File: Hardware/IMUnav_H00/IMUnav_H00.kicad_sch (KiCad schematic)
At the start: 11 parts, among them U7 STM32G474VETx

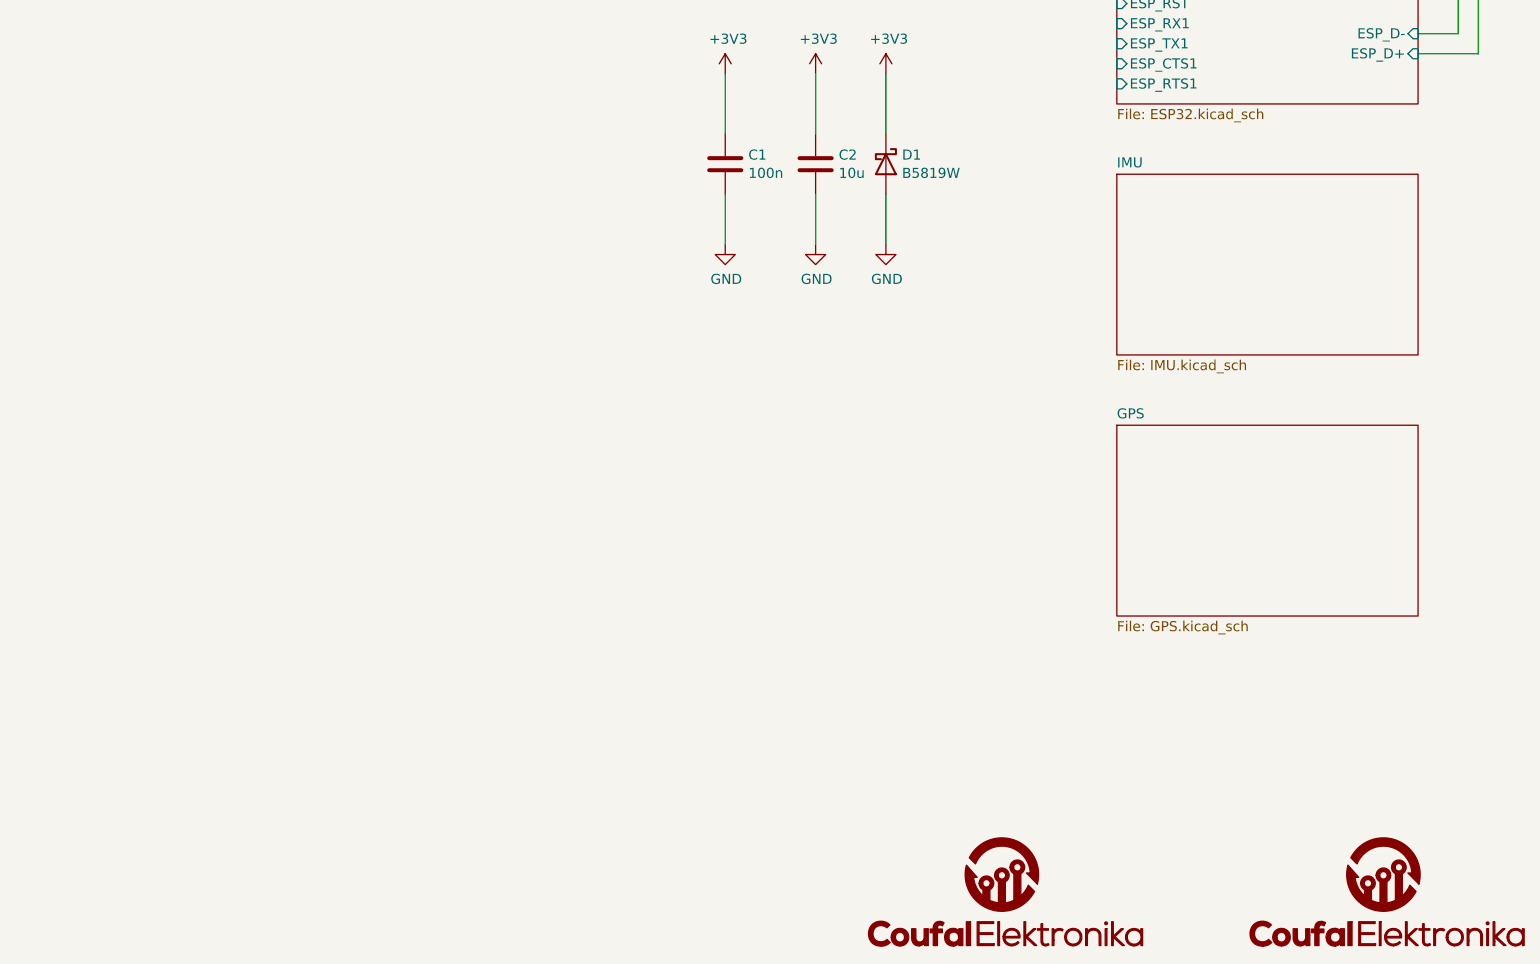
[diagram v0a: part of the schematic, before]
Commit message: Added IMU connection, created symbol for ADIS16505 PCB version
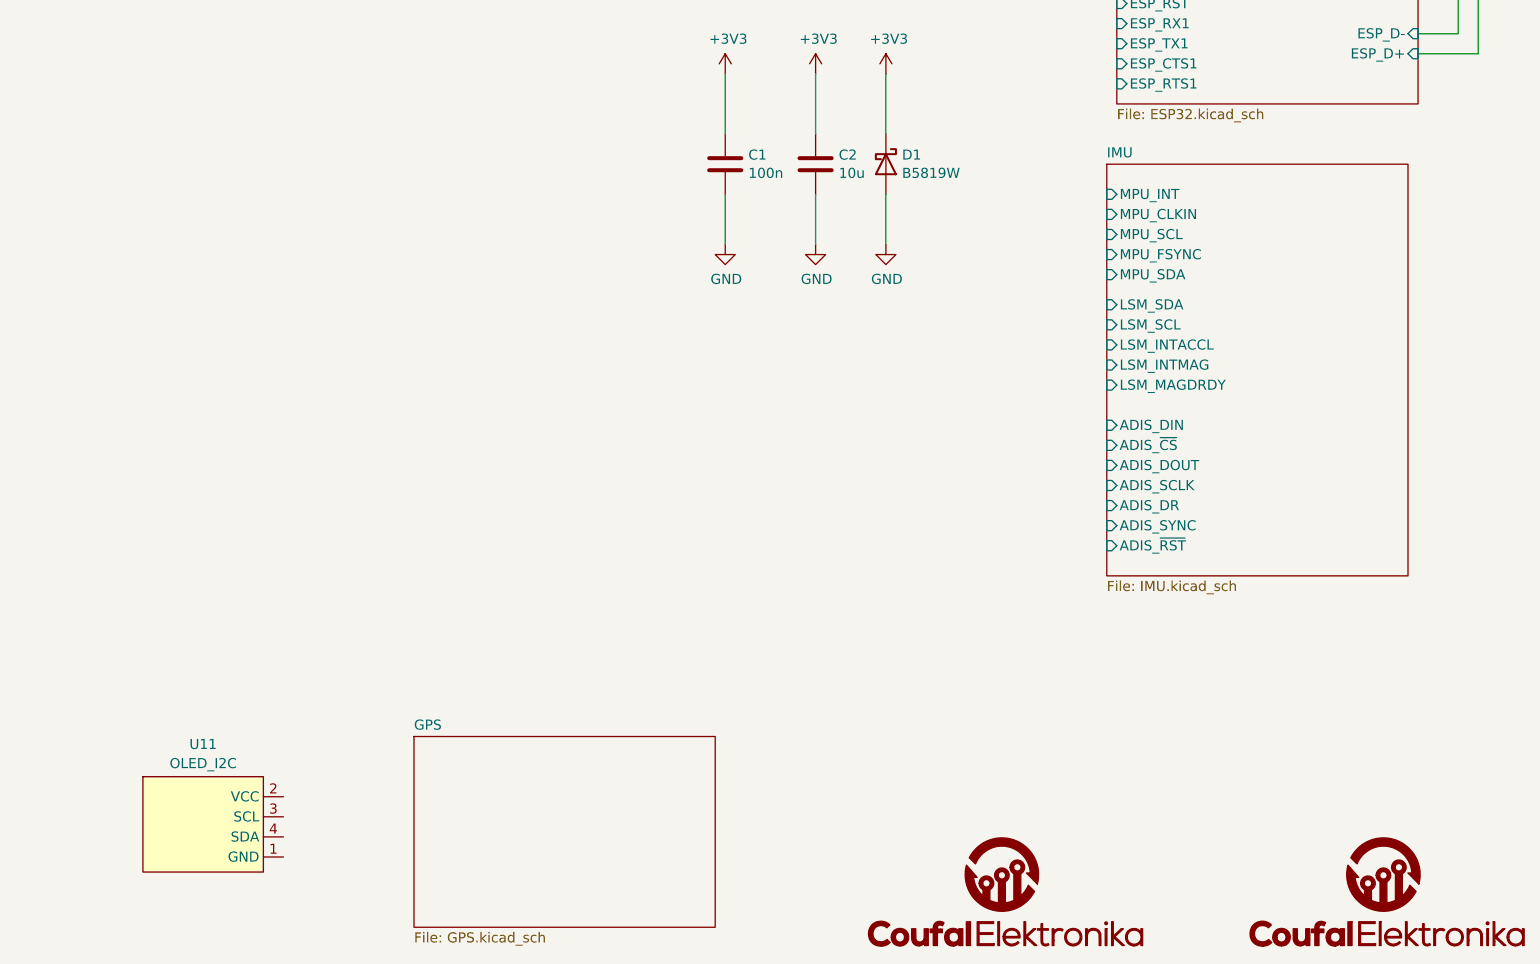
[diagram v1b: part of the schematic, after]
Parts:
- added U11: OLED_I2C, IMUnav:Display_128x64_096_I2C, symbol IMUnav:OLED_I2C
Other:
- sheet IMU ports: added ADIS_DIN, ADIS_DOUT, ADIS_DR, ADIS_SCLK, ADIS_SYNC, ADIS_~{CS}, ADIS_~{RST}, LSM_INTACCL, LSM_INTMAG, LSM_MAGDRDY, LSM_SCL, LSM_SDA, MPU_CLKIN, MPU_FSYNC, MPU_INT, MPU_SCL, MPU_SDA; removed none
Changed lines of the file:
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@@
+    )
+  )
+  (symbol (lib_id "IMUnav:OLED_I2C") (at 110.49 165.1 0) (unit 1)
+    (in_bom yes) (on_board yes) (dnp no) (fields_autoplaced)
+    (property "Reference" "U11" (at 109.22 154.6565 0)
+      (effects (font (size 1.27 1.27)))
+    )
+    (property "Value" "OLED_I2C" (at 109.22 157.0807 0)
+      (effects (font (size 1.27 1.27)))
+    )
+    (property "Footprint" "IMUnav:Display_128x64_096_I2C" (at 95.885 159.385 0)
+      (effects (font (size 1.27 1.27)) hide)
+    )
+    (property "Datasheet" "" (at 95.885 159.385 0)
+      (effects (font (size 1.27 1.27)) hide)
+    )
+    (pin "1")
+    (pin "2")
+    (pin "3")
+    (pin "4")
+    (instances
+      (project "IMUnav_H00"
+        (path "/4c2dd95e-3649-4040-ab57-00df6d22e0b0"
+          (reference "U11") (unit 1)
+        )
+      )
     )
   )
@@
     )
   )
-  (sheet (at 224.79 82.55) (size 38.1 22.86) (fields_autoplaced)
+  (sheet (at 223.52 81.28) (size 38.1 52.07) (fields_autoplaced)
     (stroke (width 0.1524) (type solid))
     (fill (color 0 0 0 0.0000))
-    (property "Sheetname" "IMU" (at 224.79 81.8384 0)
+    (property "Sheetname" "IMU" (at 223.52 80.5684 0)
       (effects (font (size 1.27 1.27)) (justify left bottom))
     )
-    (property "Sheetfile" "IMU.kicad_sch" (at 224.79 105.9946 0)
+    (property "Sheetfile" "IMU.kicad_sch" (at 223.52 133.9346 0)
       (effects (font (size 1.27 1.27)) (justify left top))
     )
+    (pin "MPU_CLKIN" input (at 223.52 87.63 180)
+      (effects (font (size 1.27 1.27)) (justify left))
+    )
+    (pin "MPU_SCL" input (at 223.52 90.17 180)
+      (effects (font (size 1.27 1.27)) (justify left))
+    )
+    (pin "MPU_FSYNC" input (at 223.52 92.71 180)
+      (effects (font (size 1.27 1.27)) (justify left))
+    )
+    (pin "MPU_SDA" input (at 223.52 95.25 180)
+      (effects (font (size 1.27 1.27)) (justify left))
+    )
+    (pin "LSM_SDA" input (at 223.52 99.06 180)
+      (effects (font (size 1.27 1.27)) (justify left))
+    )
+    (pin "LSM_SCL" input (at 223.52 101.6 180)
+      (effects (font (size 1.27 1.27)) (justify left))
+    )
+    (pin "MPU_INT" input (at 223.52 85.09 180)
+      (effects (font (size 1.27 1.27)) (justify left))
+    )
+    (pin "LSM_INTACCL" input (at 223.52 104.14 180)
+      (effects (font (size 1.27 1.27)) (justify left))
+    )
+    (pin "LSM_INTMAG" input (at 223.52 106.68 180)
+      (effects (font (size 1.27 1.27)) (justify left))
+    )
+    (pin "LSM_MAGDRDY" input (at 223.52 109.22 180)
+      (effects (font (size 1.27 1.27)) (justify left))
+    )
+    (pin "ADIS_DIN" input (at 223.52 114.3 180)
+      (effects (font (size 1.27 1.27)) (justify left))
+    )
+    (pin "ADIS_~{CS}" input (at 223.52 116.84 180)
+      (effects (font (size 1.27 1.27)) (justify left))
+    )
+    (pin "ADIS_DOUT" input (at 223.52 119.38 180)
+      (effects (font (size 1.27 1.27)) (justify left))
+    )
+    (pin "ADIS_SCLK" input (at 223.52 121.92 180)
+      (effects (font (size 1.27 1.27)) (justify left))
+    )
+    (pin "ADIS_DR" input (at 223.52 124.46 180)
+      (effects (font (size 1.27 1.27)) (justify left))
+    )
+    (pin "ADIS_SYNC" input (at 223.52 127 180)
+      (effects (font (size 1.27 1.27)) (justify left))
+    )
+    (pin "ADIS_~{RST}" input (at 223.52 129.54 180)
+      (effects (font (size 1.27 1.27)) (justify left))
+    )
     (instances
       (project "IMUnav_H00"
@@
     )
   )
-  (sheet (at 224.79 114.3) (size 38.1 24.13) (fields_autoplaced)
+  (sheet (at 135.89 153.67) (size 38.1 24.13) (fields_autoplaced)
     (stroke (width 0.1524) (type solid))
     (fill (color 0 0 0 0.0000))
-    (property "Sheetname" "GPS" (at 224.79 113.5884 0)
+    (property "Sheetname" "GPS" (at 135.89 152.9584 0)
       (effects (font (size 1.27 1.27)) (justify left bottom))
     )
-    (property "Sheetfile" "GPS.kicad_sch" (at 224.79 139.0146 0)
+    (property "Sheetfile" "GPS.kicad_sch" (at 135.89 178.3846 0)
       (effects (font (size 1.27 1.27)) (justify left top))
     )

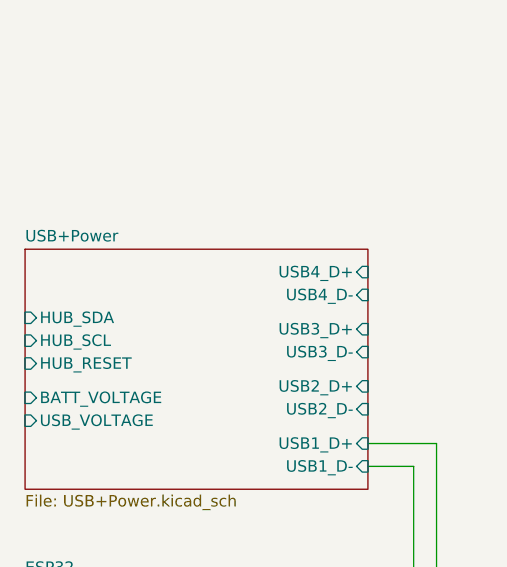
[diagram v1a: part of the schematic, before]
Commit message: Updated footprints, symbols and 3D models for ADIS165050 BGA and PCB variant
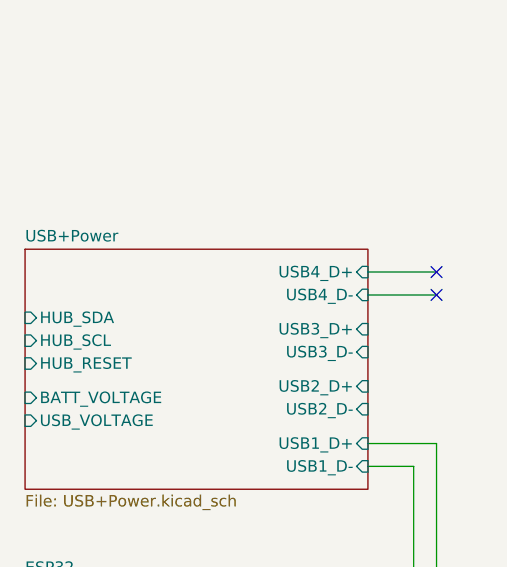
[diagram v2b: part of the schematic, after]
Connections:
- no-connect marks 0 -> 2
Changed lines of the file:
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@@
 (kicad_sch (version 20230121) (generator eeschema)
   (paper "A4")
+  (no_connect (at 270.51 26.67))
+  (no_connect (at 270.51 24.13))
   (wire (pts (xy 175.26 77.47) (xy 175.26 69.85))
     (stroke (width 0) (type default))
@@
   )
   (wire (pts (xy 175.26 85.09) (xy 175.26 91.44))
+    (stroke (width 0) (type default))
+  )
+  (wire (pts (xy 262.89 24.13) (xy 270.51 24.13))
     (stroke (width 0) (type default))
   )
@@
     (stroke (width 0) (type default))
   )
+  (wire (pts (xy 262.89 26.67) (xy 270.51 26.67))
+    (stroke (width 0) (type default))
+  )

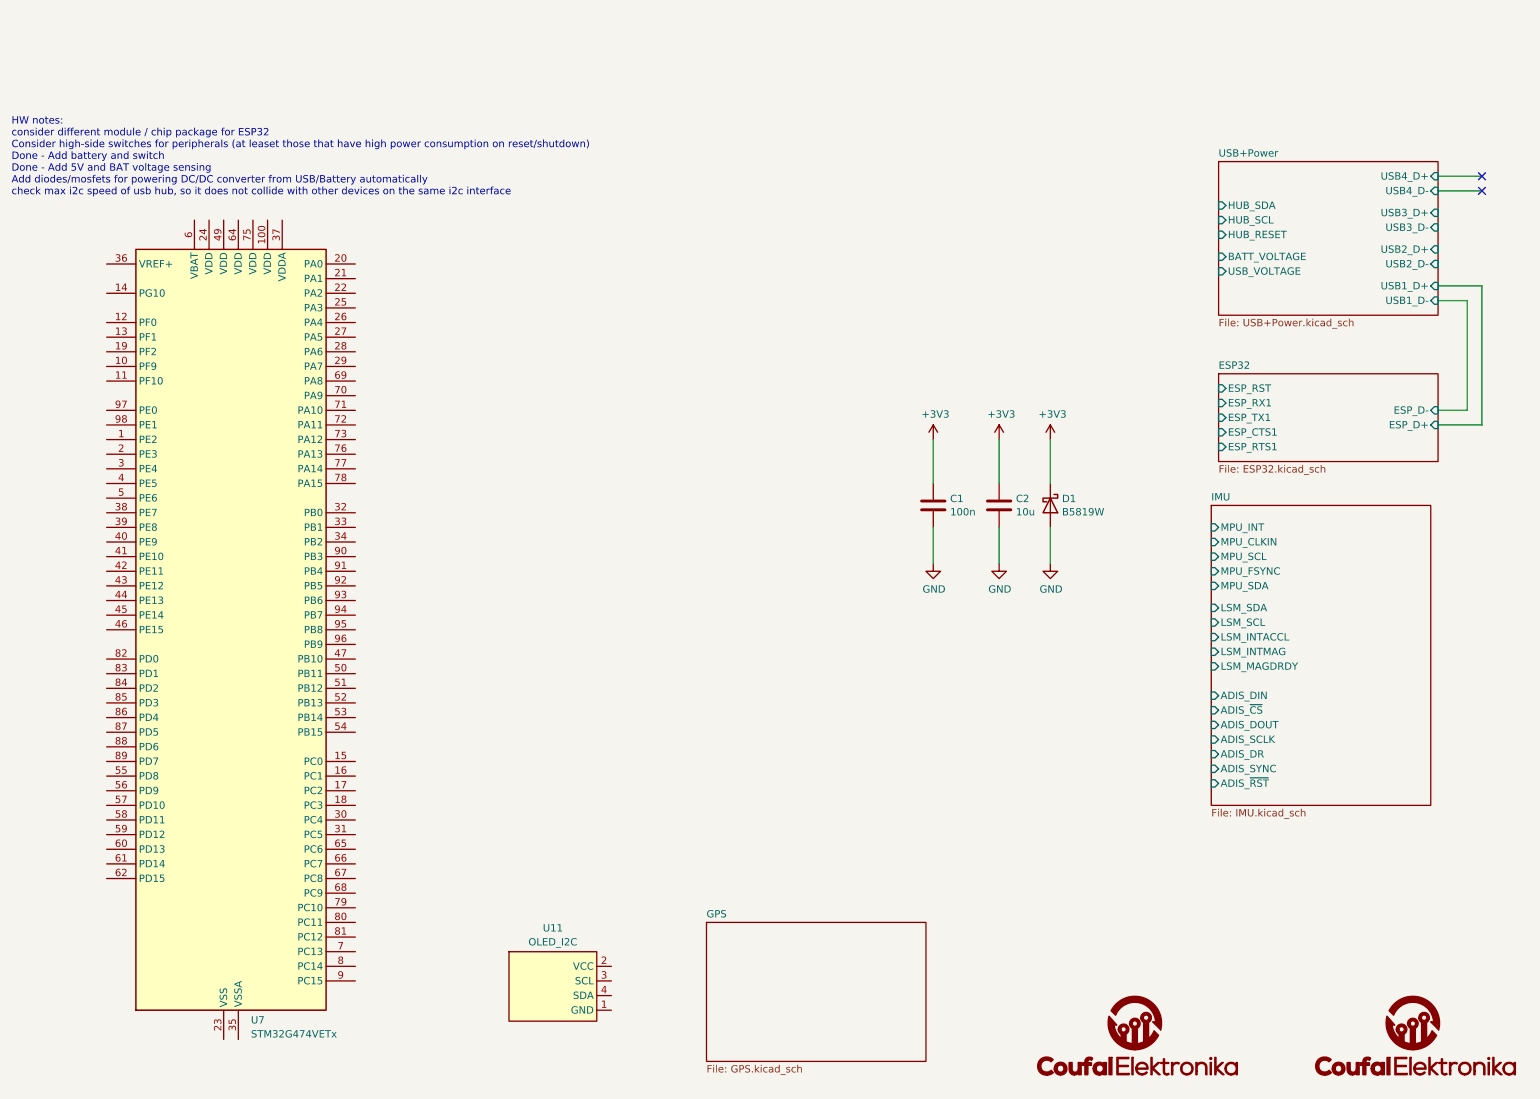
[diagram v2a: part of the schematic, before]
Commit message: Added GPS. Changes in power management.
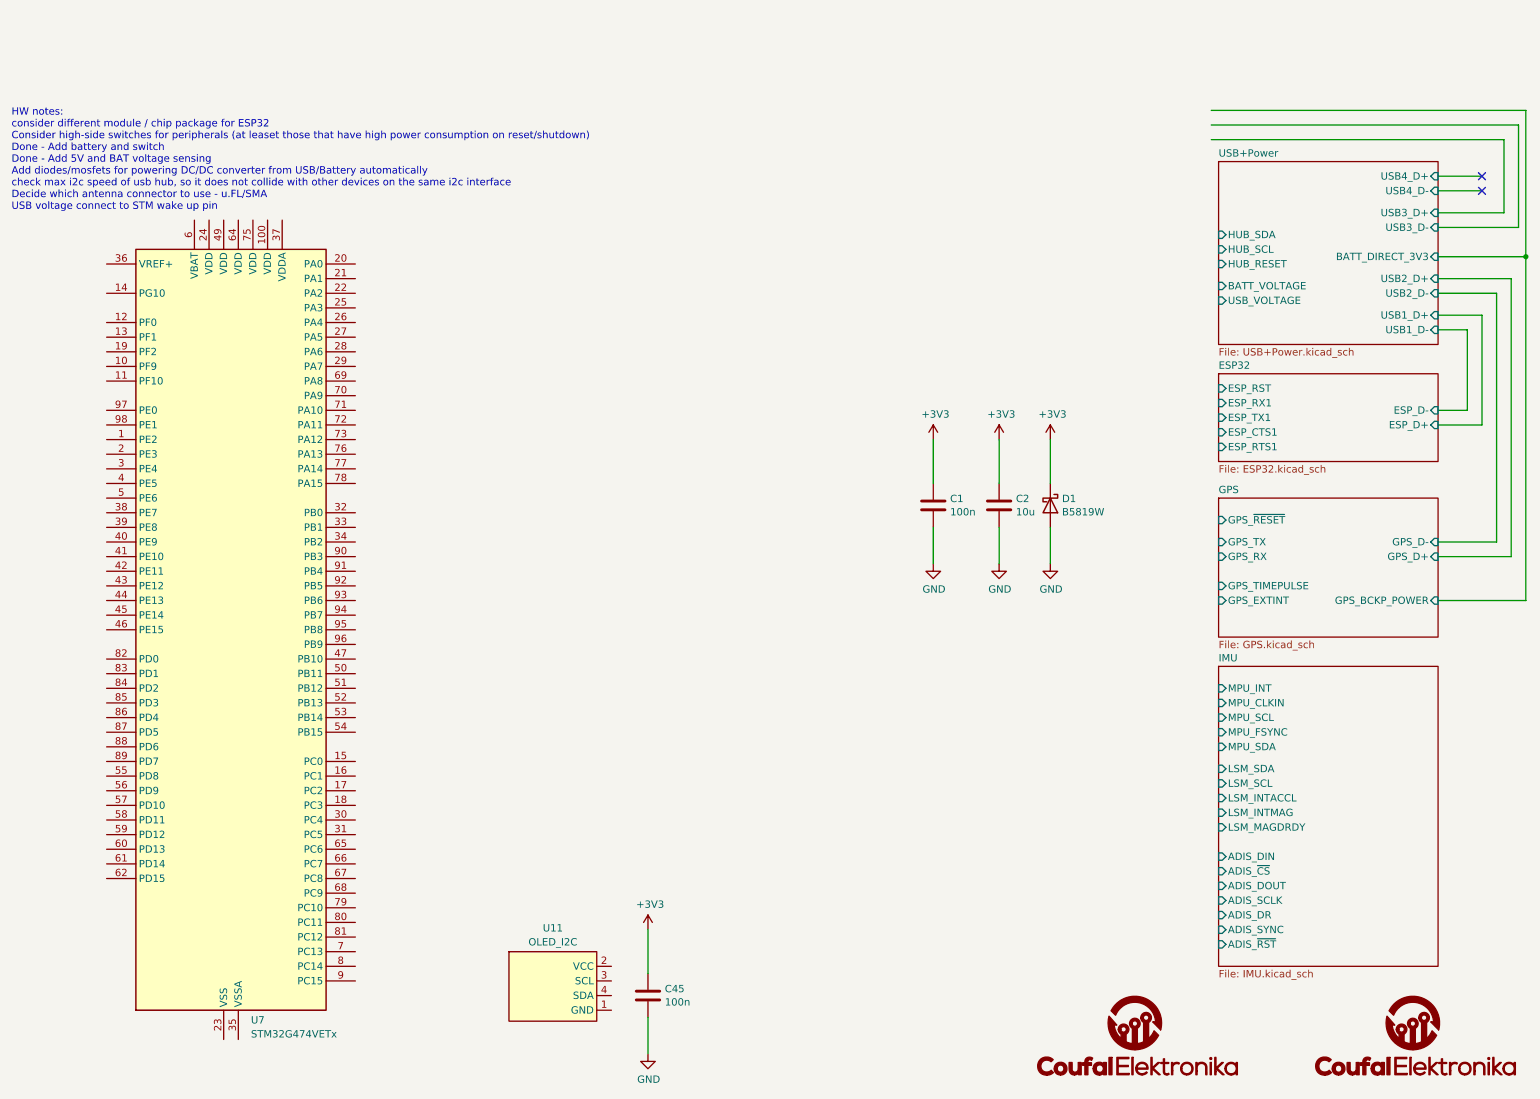
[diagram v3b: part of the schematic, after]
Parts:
- added C45: 100n, Capacitor_SMD:C_0603_1608Metric, symbol Device:C
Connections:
- net +3V3: now also C45.1
- net GND: now also C45.2
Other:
- sheet GPS ports: added GPS_BCKP_POWER, GPS_D+, GPS_D-, GPS_EXTINT, GPS_RX, GPS_TIMEPULSE, GPS_TX, GPS_~{RESET}; removed none
- sheet USB+Power ports: added BATT_DIRECT_3V3; removed none
